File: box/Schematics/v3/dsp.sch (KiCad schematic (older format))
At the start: 10 parts, among them U4 FOX924B, U5 STM32F373CCT6

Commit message: create connectors sheet
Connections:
- net CLK renamed SPI_nCLK
- net IN+ renamed ADC_IN+
- net IN- renamed ADC_IN-
- net JRST renamed JTAG_JRST
- net JTCK renamed JTAG_JTCK
- net JTDI renamed JTAG_JTDI
- net JTDO renamed JTAG_JTDO
- net JTMS renamed JTAG_JTMS
- net MISO renamed SPI_MISO
- net MOSI renamed SPI_MOSI
- net RX renamed UART_RX
- net TX renamed UART_TX
- net nCS renamed SPI_nCS
- net nRST renamed JTAG_nRST
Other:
- moved on the sheet: C20, R10

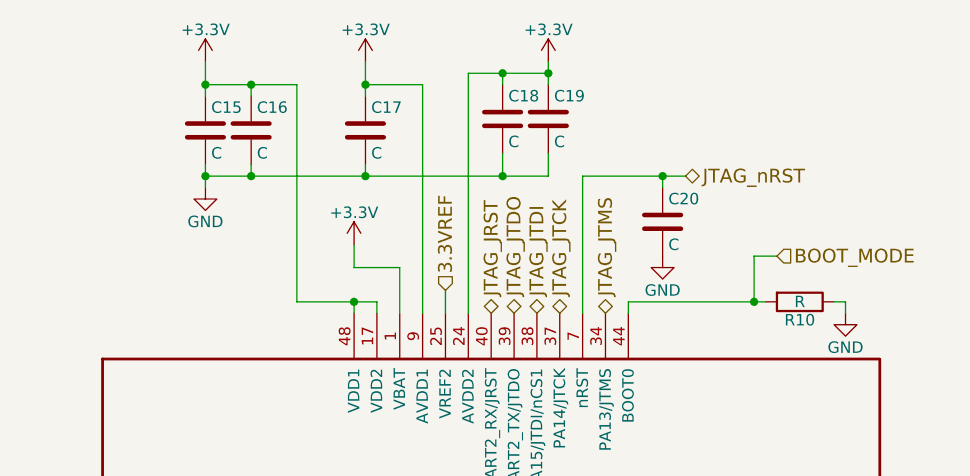
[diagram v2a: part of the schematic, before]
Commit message: add component values
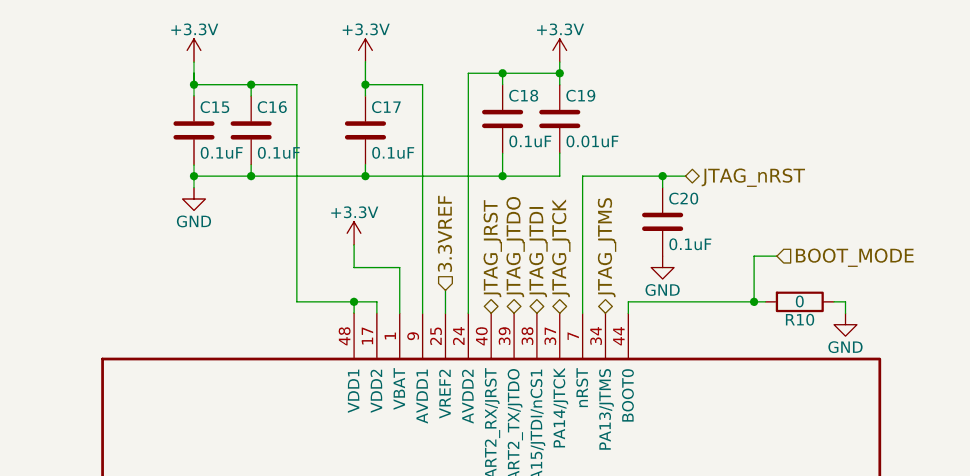
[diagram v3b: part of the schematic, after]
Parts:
- C15, C16, C17, C18, C20: value C -> 0.1uF
- C19: value C -> 0.01uF
- R10: value R -> 0
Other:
- moved on the sheet: C15, C19
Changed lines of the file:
@@
 P 6400 1650
 F 0 "C20" H 6425 1750 50  0000 L CNN
-F 1 "C" H 6425 1550 50  0000 L CNN
+F 1 "0.1uF" H 6425 1550 50  0000 L CNN
 F 2 "" H 6438 1500 50  0001 C CNN
 F 3 "" H 6400 1650 50  0001 C CNN
@@
 L C C15
 U 1 1 5A82EBD3
-P 4400 1250
-F 0 "C15" H 4425 1350 50  0000 L CNN
-F 1 "C" H 4425 1150 50  0000 L CNN
-F 2 "" H 4438 1100 50  0001 C CNN
-F 3 "" H 4400 1250 50  0001 C CNN
-	1    4400 1250
+P 4350 1250
+F 0 "C15" H 4375 1350 50  0000 L CNN
+F 1 "0.1uF" H 4375 1150 50  0000 L CNN
+F 2 "" H 4388 1100 50  0001 C CNN
+F 3 "" H 4350 1250 50  0001 C CNN
+	1    4350 1250
 	1    0    0    -1
 $EndComp
@@
 P 4600 1250
 F 0 "C16" H 4625 1350 50  0000 L CNN
-F 1 "C" H 4625 1150 50  0000 L CNN
+F 1 "0.1uF" H 4625 1150 50  0000 L CNN
 F 2 "" H 4638 1100 50  0001 C CNN
 F 3 "" H 4600 1250 50  0001 C CNN
@@
 L GND #PWR037
 U 1 1 5A82EC8F
-P 4400 1500
-F 0 "#PWR037" H 4400 1250 50  0001 C CNN
-F 1 "GND" H 4400 1350 50  0000 C CNN
-F 2 "" H 4400 1500 50  0001 C CNN
-F 3 "" H 4400 1500 50  0001 C CNN
-	1    4400 1500
+P 4350 1500
+F 0 "#PWR037" H 4350 1250 50  0001 C CNN
+F 1 "GND" H 4350 1350 50  0000 C CNN
+F 2 "" H 4350 1500 50  0001 C CNN
+F 3 "" H 4350 1500 50  0001 C CNN
+	1    4350 1500
 	1    0    0    -1
 $EndComp
@@
 L +3.3V #PWR038
 U 1 1 5A82EF25
-P 4400 950
-F 0 "#PWR038" H 4400 800 50  0001 C CNN
-F 1 "+3.3V" H 4400 1090 50  0000 C CNN
-F 2 "" H 4400 950 50  0001 C CNN
-F 3 "" H 4400 950 50  0001 C CNN
-	1    4400 950
+P 4350 950
+F 0 "#PWR038" H 4350 800 50  0001 C CNN
+F 1 "+3.3V" H 4350 1090 50  0000 C CNN
+F 2 "" H 4350 950 50  0001 C CNN
+F 3 "" H 4350 950 50  0001 C CNN
+	1    4350 950
 	1    0    0    -1
 $EndComp
@@
 P 5100 1250
 F 0 "C17" H 5125 1350 50  0000 L CNN
-F 1 "C" H 5125 1150 50  0000 L CNN
+F 1 "0.1uF" H 5125 1150 50  0000 L CNN
 F 2 "" H 5138 1100 50  0001 C CNN
 F 3 "" H 5100 1250 50  0001 C CNN
@@
 P 5700 1200
 F 0 "C18" H 5725 1300 50  0000 L CNN
-F 1 "C" H 5725 1100 50  0000 L CNN
+F 1 "0.1uF" H 5725 1100 50  0000 L CNN
 F 2 "" H 5738 1050 50  0001 C CNN
 F 3 "" H 5700 1200 50  0001 C CNN
@@
 L C C19
 U 1 1 5A82F58D
-P 5900 1200
-F 0 "C19" H 5925 1300 50  0000 L CNN
-F 1 "C" H 5925 1100 50  0000 L CNN
-F 2 "" H 5938 1050 50  0001 C CNN
-F 3 "" H 5900 1200 50  0001 C CNN
-	1    5900 1200
+P 5950 1200
+F 0 "C19" H 5975 1300 50  0000 L CNN
+F 1 "0.01uF" H 5975 1100 50  0000 L CNN
+F 2 "" H 5988 1050 50  0001 C CNN
+F 3 "" H 5950 1200 50  0001 C CNN
+	1    5950 1200
 	1    0    0    -1
 $EndComp
@@
 L +3.3V #PWR040
 U 1 1 5A82FBEF
-P 5900 950
-F 0 "#PWR040" H 5900 800 50  0001 C CNN
-F 1 "+3.3V" H 5900 1090 50  0000 C CNN
-F 2 "" H 5900 950 50  0001 C CNN
-F 3 "" H 5900 950 50  0001 C CNN
-	1    5900 950
+P 5950 950
+F 0 "#PWR040" H 5950 800 50  0001 C CNN
+F 1 "+3.3V" H 5950 1090 50  0000 C CNN
+F 2 "" H 5950 950 50  0001 C CNN
+F 3 "" H 5950 950 50  0001 C CNN
+	1    5950 950
 	1    0    0    -1
 $EndComp
@@
 P 7000 2000
 F 0 "R10" V 7080 2000 50  0000 C CNN
-F 1 "R" V 7000 2000 50  0000 C CNN
+F 1 "0" V 7000 2000 50  0000 C CNN
 F 2 "" V 6930 2000 50  0001 C CNN
 F 3 "" H 7000 2000 50  0001 C CNN
@@
 Wire Wire Line
 	5100 950  5100 1100
-Wire Wire Line
-	4400 950  4400 1100
 Connection ~ 5700 1450
 Connection ~ 5100 1450
@@
 	5350 1050 5100 1050
 Connection ~ 5700 1000
-Connection ~ 5900 1000
 Wire Wire Line
 	5700 1000 5700 1050
 Wire Wire Line
-	5550 1000 5900 1000
-Wire Wire Line
-	5900 950  5900 1050
-Wire Wire Line
-	5900 1350 5900 1450
+	5550 1000 5950 1000
 Wire Wire Line
 	5700 1450 5700 1350
@@
 	4800 1050 4800 2000
 Wire Wire Line
-	5900 1450 4400 1450
-Wire Wire Line
-	4400 1050 4800 1050
+	4350 1450 5950 1450
+Wire Wire Line
+	4350 1050 4800 1050
 Wire Wire Line
 	5550 1000 5550 2050
@@
 	5050 2050 5050 2000
 Connection ~ 4600 1050
-Connection ~ 4400 1050
 Wire Wire Line
 	4600 1050 4600 1100
-Connection ~ 4400 1450
 Wire Wire Line
 	4600 1450 4600 1400
-Wire Wire Line
-	4400 1500 4400 1400
 Wire Wire Line
 	5150 2000 5150 2050
@@
 	7200 2000 7200 2050
 Connection ~ 6800 2000
+Wire Wire Line
+	5950 950  5950 1050
+Connection ~ 5950 1000
+Wire Wire Line
+	5950 1450 5950 1350
+Wire Wire Line
+	4350 1500 4350 1400
+Connection ~ 4350 1450
+Wire Wire Line
+	4350 950  4350 1100
+Wire Wire Line
+	4350 1050 4350 1000
+Connection ~ 4350 1050
 $EndSCHEMATC

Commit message: start layout
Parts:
- removed U4: FOX924B, symbol FOX924B
- added U2: FOX924B, Oscillators:Oscillator_SMD_TXC_7C-4pin_5.0x3.2mm_HandSoldering, symbol FOX924B
- C14: value C -> 0.1uF; footprint (none) -> Capacitors_SMD:C_0402
- C15, C16, C17, C18, C19, C20: footprint (none) -> Capacitors_SMD:C_0402
- R10: footprint (none) -> Resistors_THT:R_Axial_Shunt_L22.2mm_W8.0mm_PS14.30mm_P25.40mm
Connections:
- net +3V3: now also U2.4 (VCC)
- net GND: now also U2.2 (GND)
- net at U5.5 (PF0/OSC_IN): now also U2.3 (OSC)
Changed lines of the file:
@@
 EESchema Schematic File Version 2
+LIBS:opqbox3-rescue
 LIBS:opqbox3
 LIBS:device
@@
 $EndComp
 $Comp
-L FOX924B U4
-U 1 1 5A82B512
-P 2600 3550
-F 0 "U4" H 2800 3800 60  0000 L CNN
-F 1 "FOX924B" H 2800 3700 60  0000 L CNN
-F 2 "" H 2600 3550 60  0001 C CNN
-F 3 "" H 2600 3550 60  0001 C CNN
-	1    2600 3550
-	1    0    0    -1
-$EndComp
-$Comp
 L GND #PWR033
 U 1 1 5A82B565
@@
 P 2250 3600
 F 0 "C14" H 2275 3700 50  0000 L CNN
-F 1 "C" H 2275 3500 50  0000 L CNN
-F 2 "" H 2288 3450 50  0001 C CNN
+F 1 "0.1uF" H 2275 3500 50  0000 L CNN
+F 2 "Capacitors_SMD:C_0402" H 2288 3450 50  0001 C CNN
 F 3 "" H 2250 3600 50  0001 C CNN
 	1    2250 3600
@@
 F 0 "C20" H 6425 1750 50  0000 L CNN
 F 1 "0.1uF" H 6425 1550 50  0000 L CNN
-F 2 "" H 6438 1500 50  0001 C CNN
+F 2 "Capacitors_SMD:C_0402" H 6438 1500 50  0001 C CNN
 F 3 "" H 6400 1650 50  0001 C CNN
 	1    6400 1650
@@
 F 0 "C15" H 4375 1350 50  0000 L CNN
 F 1 "0.1uF" H 4375 1150 50  0000 L CNN
-F 2 "" H 4388 1100 50  0001 C CNN
+F 2 "Capacitors_SMD:C_0402" H 4388 1100 50  0001 C CNN
 F 3 "" H 4350 1250 50  0001 C CNN
 	1    4350 1250
@@
 F 0 "C16" H 4625 1350 50  0000 L CNN
 F 1 "0.1uF" H 4625 1150 50  0000 L CNN
-F 2 "" H 4638 1100 50  0001 C CNN
+F 2 "Capacitors_SMD:C_0402" H 4638 1100 50  0001 C CNN
 F 3 "" H 4600 1250 50  0001 C CNN
 	1    4600 1250
@@
 F 0 "C17" H 5125 1350 50  0000 L CNN
 F 1 "0.1uF" H 5125 1150 50  0000 L CNN
-F 2 "" H 5138 1100 50  0001 C CNN
+F 2 "Capacitors_SMD:C_0402" H 5138 1100 50  0001 C CNN
 F 3 "" H 5100 1250 50  0001 C CNN
 	1    5100 1250
@@
 F 0 "C18" H 5725 1300 50  0000 L CNN
 F 1 "0.1uF" H 5725 1100 50  0000 L CNN
-F 2 "" H 5738 1050 50  0001 C CNN
+F 2 "Capacitors_SMD:C_0402" H 5738 1050 50  0001 C CNN
 F 3 "" H 5700 1200 50  0001 C CNN
 	1    5700 1200
@@
 F 0 "C19" H 5975 1300 50  0000 L CNN
 F 1 "0.01uF" H 5975 1100 50  0000 L CNN
-F 2 "" H 5988 1050 50  0001 C CNN
+F 2 "Capacitors_SMD:C_0402" H 5988 1050 50  0001 C CNN
 F 3 "" H 5950 1200 50  0001 C CNN
 	1    5950 1200
@@
 F 0 "R10" V 7080 2000 50  0000 C CNN
 F 1 "0" V 7000 2000 50  0000 C CNN
-F 2 "" V 6930 2000 50  0001 C CNN
+F 2 "Resistors_THT:R_Axial_Shunt_L22.2mm_W8.0mm_PS14.30mm_P25.40mm" V 6930 2000 50  0001 C CNN
 F 3 "" H 7000 2000 50  0001 C CNN
 	1    7000 2000
@@
 	4350 1050 4350 1000
 Connection ~ 4350 1050
+$Comp
+L FOX924B U2
+U 1 1 5A83A700
+P 2600 3550
+F 0 "U2" H 2800 3800 60  0000 L CNN
+F 1 "FOX924B" H 2800 3700 60  0000 L CNN
+F 2 "Oscillators:Oscillator_SMD_TXC_7C-4pin_5.0x3.2mm_HandSoldering" H 2600 3550 60  0001 C CNN
+F 3 "" H 2600 3550 60  0001 C CNN
+	1    2600 3550
+	1    0    0    -1
+$EndComp
 $EndSCHEMATC

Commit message: remove chip, replace pi
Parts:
- removed R10: 0, Resistors_THT:R_Axial_Shunt_L22.2mm_W8.0mm_PS14.30mm_P25.40mm, symbol R
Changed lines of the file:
@@
 $EndDescr
 $Comp
-L STM32F373CCT6 U5
-U 1 1 5A835F5B
-P 3750 3350
-F 0 "U5" H 3900 3600 60  0000 R CNN
-F 1 "STM32F373CCT6" H 3900 3500 60  0000 R CNN
-F 2 "Housings_QFP:LQFP-48_7x7mm_Pitch0.5mm" H 3900 3400 60  0001 R CNN
-F 3 "" H 3750 3350 60  0001 C CNN
-	1    3750 3350
-	1    0    0    -1
-$EndComp
-$Comp
-L GND #PWR023
+L GND #PWR024
 U 1 1 5A82B565
 P 2500 3850
-F 0 "#PWR023" H 2500 3600 50  0001 C CNN
+F 0 "#PWR024" H 2500 3600 50  0001 C CNN
 F 1 "GND" H 2500 3700 50  0000 C CNN
 F 2 "" H 2500 3850 50  0001 C CNN
@@
 $EndComp
 $Comp
-L +3.3V #PWR024
+L +3.3V #PWR025
 U 1 1 5A82B58A
 P 2500 3350
-F 0 "#PWR024" H 2500 3200 50  0001 C CNN
+F 0 "#PWR025" H 2500 3200 50  0001 C CNN
 F 1 "+3.3V" H 2500 3490 50  0000 C CNN
 F 2 "" H 2500 3350 50  0001 C CNN
@@
 PPS
 $Comp
-L GND #PWR025
+L GND #PWR026
 U 1 1 5A82E118
 P 5050 6000
-F 0 "#PWR025" H 5050 5750 50  0001 C CNN
+F 0 "#PWR026" H 5050 5750 50  0001 C CNN
 F 1 "GND" H 5050 5850 50  0000 C CNN
 F 2 "" H 5050 6000 50  0001 C CNN
@@
 $EndComp
 $Comp
-L GND #PWR026
+L GND #PWR027
 U 1 1 5A82E58F
 P 6400 1800
-F 0 "#PWR026" H 6400 1550 50  0001 C CNN
+F 0 "#PWR027" H 6400 1550 50  0001 C CNN
 F 1 "GND" H 6400 1650 50  0000 C CNN
 F 2 "" H 6400 1800 50  0001 C CNN
@@
 	1    0    0    -1
 $EndComp
-Text HLabel 6900 1800 2    60   Input ~ 0
+Text HLabel 6800 2000 2    60   Input ~ 0
 BOOT_MODE
 $Comp
@@
 $EndComp
 $Comp
-L GND #PWR027
+L GND #PWR028
 U 1 1 5A82EC8F
 P 4350 1500
-F 0 "#PWR027" H 4350 1250 50  0001 C CNN
+F 0 "#PWR028" H 4350 1250 50  0001 C CNN
 F 1 "GND" H 4350 1350 50  0000 C CNN
 F 2 "" H 4350 1500 50  0001 C CNN
@@
 $EndComp
 $Comp
-L +3.3V #PWR028
+L +3.3V #PWR029
 U 1 1 5A82EF25
 P 4350 950
-F 0 "#PWR028" H 4350 800 50  0001 C CNN
+F 0 "#PWR029" H 4350 800 50  0001 C CNN
 F 1 "+3.3V" H 4350 1090 50  0000 C CNN
 F 2 "" H 4350 950 50  0001 C CNN
@@
 $EndComp
 $Comp
-L +3.3V #PWR029
+L +3.3V #PWR030
 U 1 1 5A82FBC9
 P 5100 950
-F 0 "#PWR029" H 5100 800 50  0001 C CNN
+F 0 "#PWR030" H 5100 800 50  0001 C CNN
 F 1 "+3.3V" H 5100 1090 50  0000 C CNN
 F 2 "" H 5100 950 50  0001 C CNN
@@
 $EndComp
 $Comp
-L +3.3V #PWR030
+L +3.3V #PWR031
 U 1 1 5A82FBEF
 P 5950 950
-F 0 "#PWR030" H 5950 800 50  0001 C CNN
+F 0 "#PWR031" H 5950 800 50  0001 C CNN
 F 1 "+3.3V" H 5950 1090 50  0000 C CNN
 F 2 "" H 5950 950 50  0001 C CNN
@@
 Text HLabel 3600 3850 0    60   BiDi ~ 0
 FLAG1
-$Comp
-L R R10
-U 1 1 5A831E95
-P 7000 2000
-F 0 "R10" V 7080 2000 50  0000 C CNN
-F 1 "0" V 7000 2000 50  0000 C CNN
-F 2 "Resistors_THT:R_Axial_Shunt_L22.2mm_W8.0mm_PS14.30mm_P25.40mm" V 6930 2000 50  0001 C CNN
-F 3 "" H 7000 2000 50  0001 C CNN
-	1    7000 2000
-	0    1    1    0
-$EndComp
-$Comp
-L GND #PWR031
-U 1 1 5A831ECA
-P 7200 2050
-F 0 "#PWR031" H 7200 1800 50  0001 C CNN
-F 1 "GND" H 7200 1900 50  0000 C CNN
-F 2 "" H 7200 2050 50  0001 C CNN
-F 3 "" H 7200 2050 50  0001 C CNN
-	1    7200 2050
-	1    0    0    -1
-$EndComp
 Text HLabel 3750 4450 0    60   Input ~ 0
 ADC_IN+
@@
 	1    0    0    -1
 $EndComp
-Wire Wire Line
-	6800 1800 6800 2000
-Wire Wire Line
-	6900 1800 6800 1800
 Connection ~ 6400 1450
 Wire Wire Line
@@
 	6250 2050 6250 2000
 Wire Wire Line
-	6250 2000 6850 2000
-Wire Wire Line
-	7150 2000 7200 2000
-Wire Wire Line
-	7200 2000 7200 2050
-Connection ~ 6800 2000
-Wire Wire Line
 	5950 950  5950 1050
 Connection ~ 5950 1000
@@
 	5050 1750 5050 1850
 $Comp
-L +3.3V #PWR041
+L +3.3V #PWR032
 U 1 1 5A8304E4
 P 5050 1750
-F 0 "#PWR041" H 5050 1600 50  0001 C CNN
+F 0 "#PWR032" H 5050 1600 50  0001 C CNN
 F 1 "+3.3V" H 5050 1890 50  0000 C CNN
 F 2 "" H 5050 1750 50  0001 C CNN
@@
 	1    0    0    -1
 $EndComp
+$Comp
+L STM32F373CCT6 U5
+U 1 1 5A835F5B
+P 3750 3350
+F 0 "U5" H 3900 3600 60  0000 R CNN
+F 1 "STM32F373CCT6" H 3900 3500 60  0000 R CNN
+F 2 "Housings_QFP:LQFP-48_7x7mm_Pitch0.5mm" H 3900 3400 60  0001 R CNN
+F 3 "" H 3750 3350 60  0001 C CNN
+	1    3750 3350
+	1    0    0    -1
+$EndComp
+Wire Wire Line
+	6250 2000 6800 2000
 $EndSCHEMATC
